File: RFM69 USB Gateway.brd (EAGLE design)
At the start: 46.1 x 17.2 mm, 25 parts, among them CN1 MINIB, IC3 MCP1703CB, U1 FT231XS, X1 16 MHz

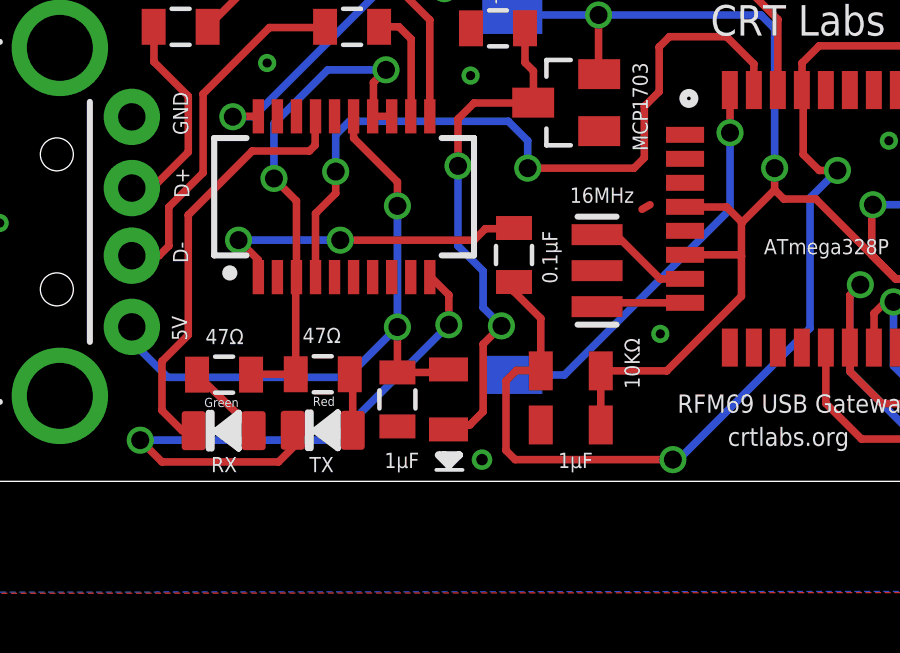
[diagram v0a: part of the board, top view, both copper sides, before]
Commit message: Minor silkscreen adjustments
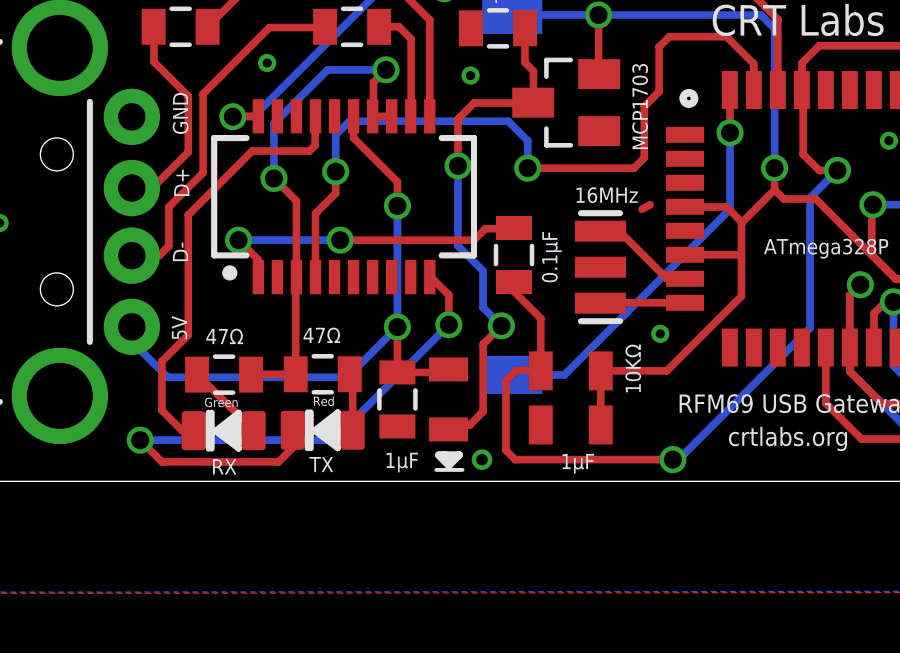
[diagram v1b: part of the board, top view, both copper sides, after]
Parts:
- moved X1 0.16 mm to (33.0, 10.1)
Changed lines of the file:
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@@
 <text x="19.812" y="7.5057" size="0.508" layer="121" font="vector">47Ω</text>
 <text x="23.0505" y="7.5438" size="0.508" layer="121" font="vector">47Ω</text>
-<text x="34.29" y="6.0198" size="0.508" layer="121" font="vector" rot="R90">10KΩ</text>
+<text x="34.3281" y="5.8293" size="0.508" layer="121" font="vector" rot="R90">10KΩ</text>
 <text x="50.4825" y="5.2578" size="0.508" layer="121" font="vector">1KΩ</text>
 <text x="26.9367" y="3.8862" size="0.508" layer="121" font="vector" rot="R180">1μF</text>
-<text x="32.7279" y="3.8862" size="0.508" layer="121" font="vector" rot="R180">1μF</text>
+<text x="32.8041" y="3.8481" size="0.508" layer="121" font="vector" rot="R180">1μF</text>
 <text x="52.0065" y="17.8689" size="0.508" layer="121" font="vector" rot="R180">0.1μF</text>
 <text x="29.0322" y="19.0119" size="0.508" layer="121" font="vector">1μF</text>
-<text x="20.0025" y="3.2385" size="0.508" layer="121" font="vector">RX</text>
+<text x="20.0025" y="3.1623" size="0.508" layer="121" font="vector">RX</text>
 <text x="23.2791" y="3.2385" size="0.508" layer="121" font="vector">TX</text>
 <text x="19.7739" y="5.4102" size="0.3048" layer="121" font="vector">Green</text>
 <text x="23.3934" y="5.4483" size="0.3048" layer="121" font="vector">Red</text>
-<text x="34.0995" y="12.7254" size="0.508" layer="121" font="vector" rot="R180">16MHz</text>
+<text x="34.2519" y="12.7254" size="0.508" layer="121" font="vector" rot="R180">16MHz</text>
 <text x="34.5567" y="13.9446" size="0.508" layer="121" font="vector" rot="R90">MCP1703</text>
 <text x="54.5592" y="5.334" size="0.3048" layer="121" font="vector">Status LED</text>
@@
 </autorouter>
 <elements>
-<element name="X1" library="SparkFun" package="RESONATOR-SMD" value="16 MHz" x="32.8676" y="9.9568" smashed="yes" rot="R270"/>
+<element name="X1" library="SparkFun" package="RESONATOR-SMD" value="16 MHz" x="32.9819" y="10.0711" smashed="yes" rot="R270"/>
 <element name="IC3" library="linear" package="SOT23" value="MCP1703CB" x="31.8389" y="15.5575" smashed="yes" rot="R90"/>
 <element name="ATMEGA328" library="LowPowerLab" package="TQFP32-08" value="ATMega-328" x="40.0939" y="11.684" smashed="yes"/>
@@
 <contactref element="X1" pad="1"/>
 <contactref element="ATMEGA328" pad="7"/>
-<wire x1="32.8676" y1="11.1568" x2="33.4964" y2="11.1568" width="0.254" layer="1"/>
-<wire x1="33.4964" y1="11.1568" x2="34.9758" y2="9.6774" width="0.254" layer="1"/>
-<wire x1="34.9758" y1="9.6774" x2="35.7947" y2="9.6774" width="0.254" layer="1"/>
 <wire x1="35.7947" y1="9.6774" x2="35.8013" y2="9.684" width="0.254" layer="1"/>
+<wire x1="35.8013" y1="9.684" x2="35.1978" y2="9.684" width="0.254" layer="1"/>
+<wire x1="35.1978" y1="9.684" x2="33.6042" y2="11.2776" width="0.254" layer="1"/>
+<wire x1="33.6042" y1="11.2776" x2="32.9884" y2="11.2776" width="0.254" layer="1"/>
+<wire x1="32.9884" y1="11.2776" x2="32.9819" y2="11.2711" width="0.254" layer="1"/>
 </signal>
 <signal name="N$21">
 <contactref element="X1" pad="3"/>
 <contactref element="ATMEGA328" pad="8"/>
-<wire x1="32.8043" y1="8.884" x2="32.8676" y2="8.7568" width="0.254" layer="1"/>
-<wire x1="35.8013" y1="8.884" x2="33.0329" y2="8.884" width="0.254" layer="1"/>
-<wire x1="33.0329" y1="8.884" x2="32.8676" y2="8.7568" width="0.254" layer="1"/>
+<wire x1="32.8043" y1="8.884" x2="32.9819" y2="8.8711" width="0.254" layer="1"/>
+<wire x1="35.8013" y1="8.884" x2="32.9948" y2="8.884" width="0.254" layer="1"/>
+<wire x1="32.9948" y1="8.884" x2="32.9819" y2="8.8711" width="0.254" layer="1"/>
 </signal>
 <signal name="AREF">

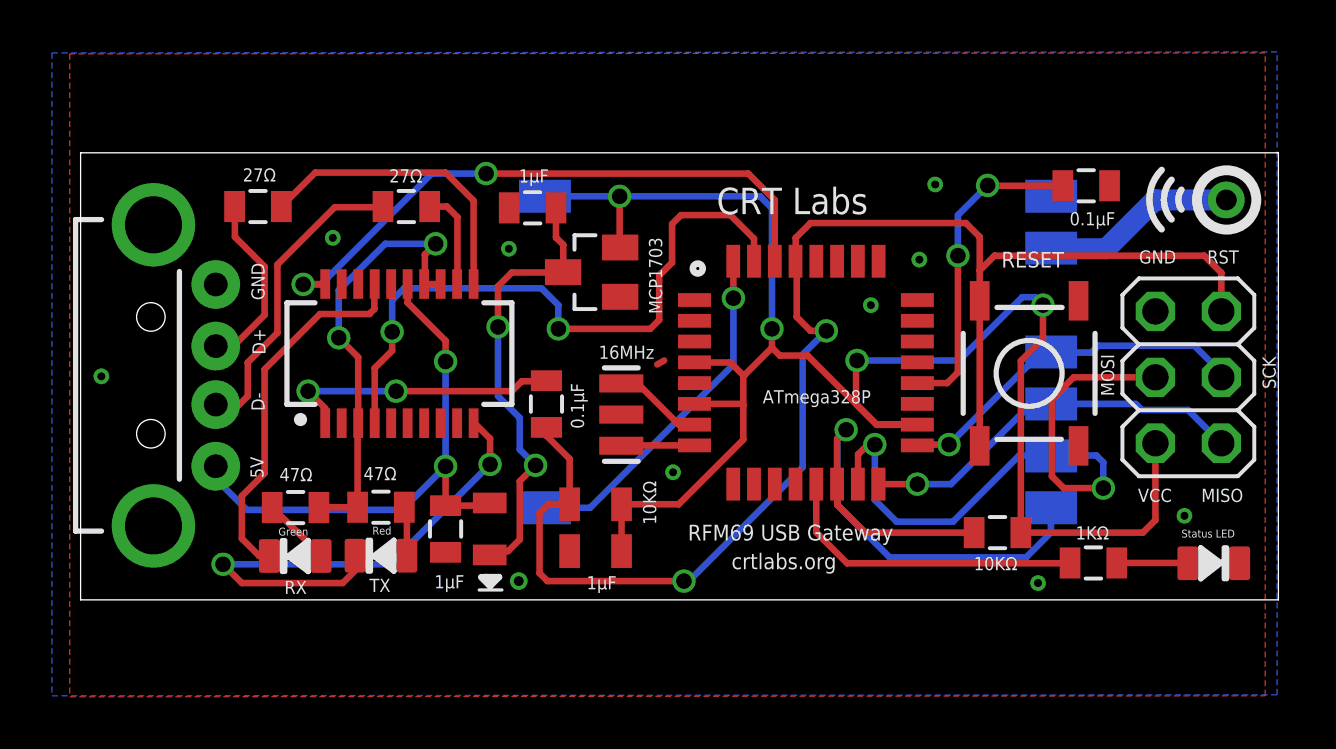
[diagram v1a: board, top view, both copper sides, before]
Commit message: Added CRT Labs logo
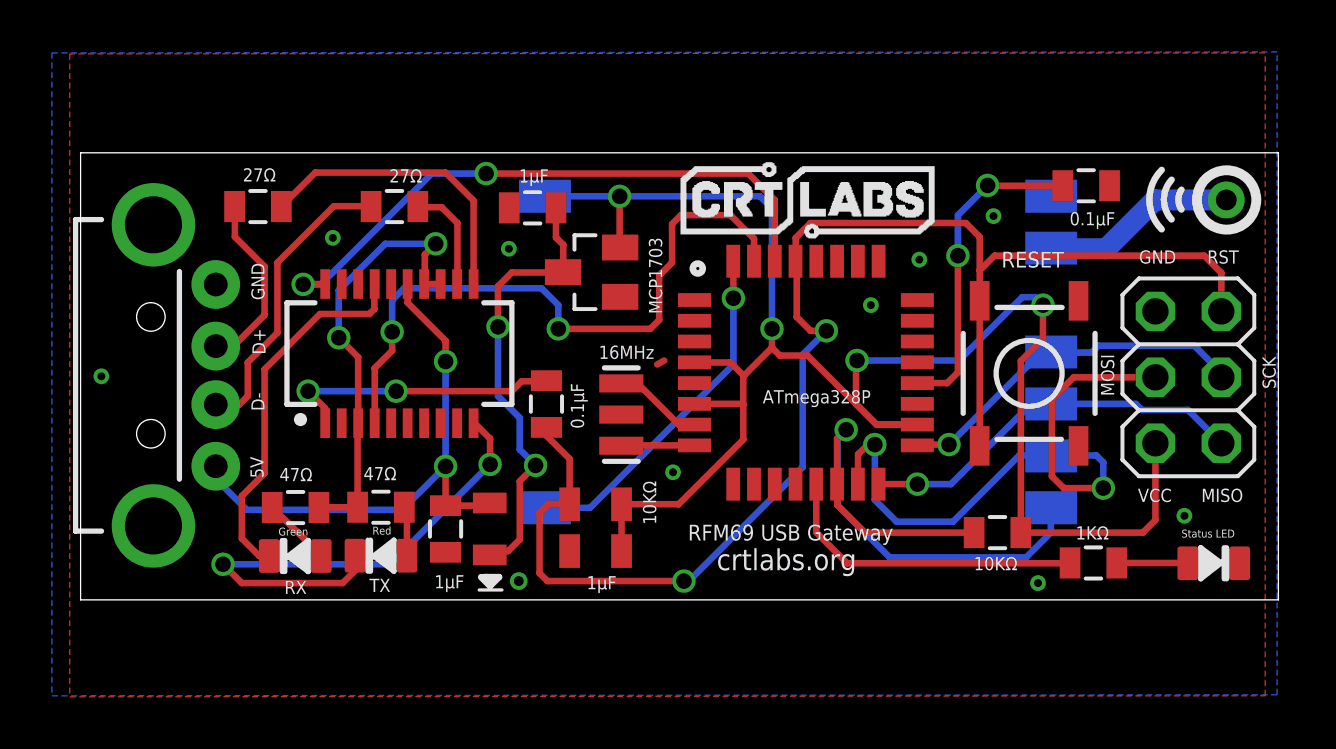
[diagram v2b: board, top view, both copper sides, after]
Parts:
- moved R3 0.46 mm to (24.2, 18.1)
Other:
- board text removed: "CRT Labs"
